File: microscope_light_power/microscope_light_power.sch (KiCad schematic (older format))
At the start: 36 parts, among them IC1 TPS61090, J1 MICROUSB, J2 5V175_out, J3 enable_switch, U1 MCP73871-2AA

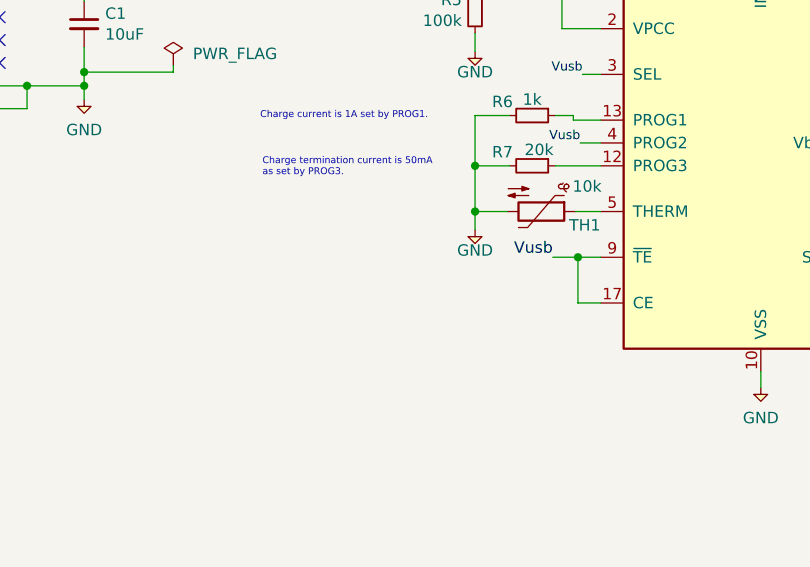
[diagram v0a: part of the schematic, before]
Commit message: Routed all of the direct connections from the MCP73871. I also added a note about the very bizarre routing for the thermistor. By the time I realized its trace would have to go on the bottom a good chunk of this board was routed. I routed it along the outside of the board to prevent breaking up the ground plane.
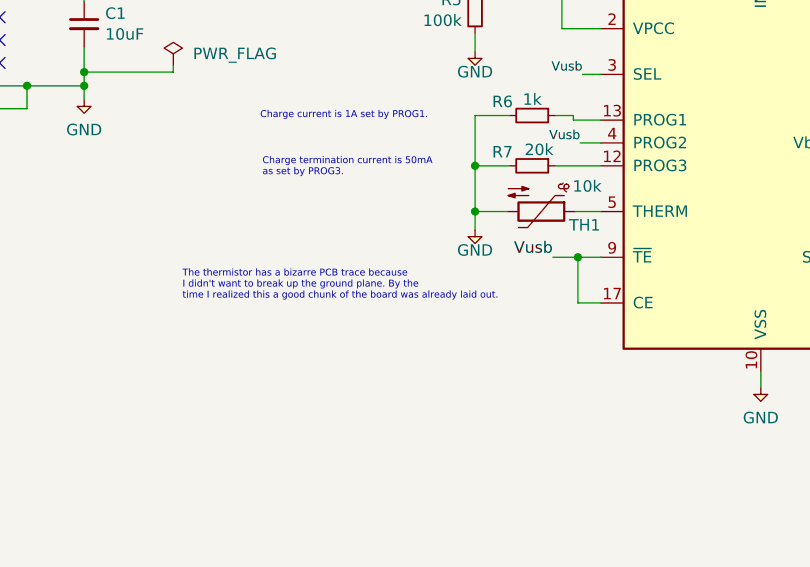
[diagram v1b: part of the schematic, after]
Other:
- note added: "The thermistor has a bizarre PCB trace because \nI didn't want to break up the ground plane. By the \ntime I realized this a good chunk of the board was already laid out."
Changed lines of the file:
@@
 Text Label 3250 4900 0    30   ~ 0
 SW
+Text Notes 2430 2750 0    30   ~ 0
+The thermistor has a bizarre PCB trace because \nI didn't want to break up the ground plane. By the \ntime I realized this a good chunk of the board was already laid out.
 $EndSCHEMATC

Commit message: Change the TPS61090 annotation from IC* to U* and move the reference designator on to the silkscreen layer.
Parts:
- renumbered IC1 to U2
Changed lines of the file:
@@
 $EndDescr
 $Comp
-L TPS61090 IC1
+L TPS61090 U2
 U 1 1 59D90497
 P 3700 5600
-F 0 "IC1" H 3700 6525 50  0000 C CNN
+F 0 "U2" H 3700 6525 50  0000 C CNN
 F 1 "TPS61090" H 3700 6434 50  0000 C CNN
 F 2 "agg:QFN-16-EP-TI" H 3400 4700 50  0001 L CNN

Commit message: Updated TPS61090 footprint to the correct footprint and modified the symbol to match KLC. sym-lib-table is due to a recent change in KiCad.
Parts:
- removed U2: TPS61090, agg:QFN-16-EP-TI, symbol TPS61090
- added U2: TPS61090, Housings_DFN_QFN:QFN-16-1EP_4x4mm_Pitch0.65mm, symbol dc-dc:TPS61090
- J1: symbol MICROUSB -> agg-kicad:MICROUSB
- J2, J3: symbol CONN_01x02 -> agg-kicad:CONN_01x02
- TP1, TP2, TP3, TP4: symbol TESTPAD -> agg-kicad:TESTPAD
- green1, yellow1: symbol LED -> agg-kicad:LED
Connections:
- wire segments 98 -> 99
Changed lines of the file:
@@
-EESchema Schematic File Version 3
-LIBS:agg-kicad
-LIBS:zetex
-LIBS:wiznet
-LIBS:triac_thyristor
-LIBS:nxp
-LIBS:modules
-LIBS:logic_programmable
-LIBS:intersil
-LIBS:infineon
-LIBS:driver_gate
-LIBS:bosch
-LIBS:bbd
-LIBS:Worldsemi
-LIBS:Valve
-LIBS:Transistor
-LIBS:Transformer
-LIBS:Switch
-LIBS:Sensor_Current
-LIBS:Relay
-LIBS:RFSolutions
-LIBS:Motor
-LIBS:Mechanical
-LIBS:MCU_Texas_MSP430
-LIBS:MCU_ST_STM8
-LIBS:MCU_ST_STM32
-LIBS:MCU_NXP_S08
-LIBS:MCU_NXP_LPC
-LIBS:MCU_NXP_Kinetis
-LIBS:MCU_Microchip_PIC32
-LIBS:MCU_Microchip_PIC24
-LIBS:MCU_Microchip_PIC18
-LIBS:MCU_Microchip_PIC16
-LIBS:MCU_Microchip_PIC12
-LIBS:MCU_Microchip_PIC10
-LIBS:Logic_TTL_IEEE
-LIBS:Logic_CMOS_IEEE
-LIBS:Logic_CMOS_4000
-LIBS:Logic_74xx
-LIBS:Logic_74xgxx
-LIBS:LEM
-LIBS:LED
-LIBS:Graphic
-LIBS:FPGA_Actel
-LIBS:Espressif
-LIBS:Display
-LIBS:Diode
-LIBS:DSP_Microchip_DSPIC33
-LIBS:Connector
-LIBS:Battery_Management
-LIBS:ftdi
-LIBS:intel
-LIBS:motor_drivers
-LIBS:references
-LIBS:maxim
-LIBS:opto
-LIBS:philips
-LIBS:pspice
-LIBS:xilinx
-LIBS:onsemi
-LIBS:digital-audio
-LIBS:interface
-LIBS:Oscillators
-LIBS:nordicsemi
-LIBS:sensors
-LIBS:contrib
-LIBS:video
-LIBS:ir
-LIBS:analog_switches
-LIBS:device
-LIBS:ESD_Protection
-LIBS:Altera
-LIBS:linear
-LIBS:atmel
-LIBS:supertex
-LIBS:siliconi
-LIBS:silabs
-LIBS:regul
-LIBS:memory
-LIBS:dsp
-LIBS:power
-LIBS:microchip
-LIBS:rfcom
-LIBS:ac-dc
-LIBS:Xicor
-LIBS:texas
-LIBS:Power_Management
-LIBS:hc11
-LIBS:analog_devices
-LIBS:dc-dc
-LIBS:powerint
-LIBS:elec-unifil
-LIBS:Zilog
-LIBS:adc-dac
-LIBS:motorola
-LIBS:Lattice
-LIBS:cypress
-LIBS:audio
-LIBS:microcontrollers
-LIBS:transistors
-LIBS:display
-LIBS:microchip_pic32mcu
-LIBS:microchip_dspic33dsc
-LIBS:conn
-LIBS:switches
-LIBS:graphic
-LIBS:nxp_armmcu
-LIBS:microchip_pic18mcu
-LIBS:74xgxx
-LIBS:cmos_ieee
-LIBS:diode
-LIBS:ttl_ieee
-LIBS:msp430
-LIBS:brooktre
-LIBS:microchip_pic10mcu
-LIBS:relays
-LIBS:stm8
-LIBS:valves
-LIBS:cmos4000
-LIBS:actel
-LIBS:stm32
-LIBS:logo
-LIBS:gennum
-LIBS:microchip_pic12mcu
-LIBS:74xx
-LIBS:transf
-LIBS:microchip_pic16mcu
+EESchema Schematic File Version 4
 LIBS:microscope_light_power-cache
 EELAYER 26 0
@@
 $EndDescr
 $Comp
-L TPS61090 U2
-U 1 1 59D90497
-P 3700 5600
-F 0 "U2" H 3700 6525 50  0000 C CNN
-F 1 "TPS61090" H 3700 6434 50  0000 C CNN
-F 2 "agg:QFN-16-EP-TI" H 3400 4700 50  0001 L CNN
-F 3 "http://www.ti.com/lit/ds/symlink/tps61090.pdf" H 3400 4600 50  0001 L CNN
-	1    3700 5600
-	1    0    0    -1
-$EndComp
-$Comp
 L MCP73871-2AA U1
 U 1 1 59D910F2
@@
 $EndComp
 $Comp
-L MICROUSB J1
+L agg-kicad:MICROUSB J1
 U 1 1 59D91D50
 P 1330 1610
@@
 $EndComp
 $Comp
-L GND #PWR01
+L agg-kicad:GND #PWR01
 U 1 1 59D99426
 P 2000 1870
@@
 Vusb
 $Comp
-L GND #PWR02
+L agg-kicad:GND #PWR02
 U 1 1 59D9AC2B
 P 3710 1660
@@
 $EndComp
 $Comp
-L GND #PWR03
+L agg-kicad:GND #PWR03
 U 1 1 59D9FB5D
 P 4960 3130
@@
 $EndComp
 $Comp
-L GND #PWR04
+L agg-kicad:GND #PWR04
 U 1 1 59DA04A7
 P 6480 2310
@@
 $EndComp
 $Comp
-L GND #PWR05
+L agg-kicad:GND #PWR05
 U 1 1 59DA245E
 P 3710 2440
@@
 Vusb
 $Comp
-L LED yellow1
+L agg-kicad:LED yellow1
 U 1 1 59DA5C71
 P 6050 2560
@@
 $EndComp
 $Comp
-L LED green1
+L agg-kicad:LED green1
 U 1 1 59DA7F2A
 P 6050 2660
@@
 $EndComp
 $Comp
-L GND #PWR06
+L agg-kicad:GND #PWR06
 U 1 1 59DCA58C
 P 6260 1750
@@
 enable
 $Comp
-L GND #PWR07
+L agg-kicad:GND #PWR07
 U 1 1 59EF0E02
 P 2330 5720
@@
 5V175
 $Comp
-L GND #PWR08
+L agg-kicad:GND #PWR08
 U 1 1 59F01C50
 P 4640 5610
@@
 $EndComp
 $Comp
-L GND #PWR09
+L agg-kicad:GND #PWR09
 U 1 1 59F0FE60
 P 2080 5260
@@
 $EndComp
 $Comp
-L GND #PWR010
+L agg-kicad:GND #PWR010
 U 1 1 59F358E1
 P 5200 5330
@@
 $EndComp
 $Comp
-L GND #PWR011
+L agg-kicad:GND #PWR011
 U 1 1 59F37EA3
-P 3130 6430
-F 0 "#PWR011" H 3000 6470 50  0001 L CNN
-F 1 "GND" H 3130 6297 50  0000 C CNN
-F 2 "" H 3130 6430 50  0001 C CNN
-F 3 "" H 3130 6430 50  0001 C CNN
-	1    3130 6430
+P 3750 6130
+F 0 "#PWR011" H 3620 6170 50  0001 L CNN
+F 1 "GND" H 3750 5997 50  0000 C CNN
+F 2 "" H 3750 6130 50  0001 C CNN
+F 3 "" H 3750 6130 50  0001 C CNN
+	1    3750 6130
 	1    0    0    -1
 $EndComp
@@
 	5200 5330 5200 5270
 Connection ~ 5200 5270
-Wire Wire Line
-	3300 5800 3130 5800
-Wire Wire Line
-	3130 5800 3130 6430
-Wire Wire Line
-	3300 5900 3130 5900
-Connection ~ 3130 5900
-Wire Wire Line
-	3300 6000 3130 6000
-Connection ~ 3130 6000
-Wire Wire Line
-	3300 6100 3130 6100
-Connection ~ 3130 6100
-Wire Wire Line
-	3300 6200 3130 6200
-Connection ~ 3130 6200
 $Comp
 L Mounting_Hole MK3
@@
 $EndComp
 $Comp
-L CONN_01x02 J3
+L agg-kicad:CONN_01x02 J3
 U 1 1 59FBD39A
 P 6370 5580
@@
 $EndComp
 $Comp
-L CONN_01x02 J2
+L agg-kicad:CONN_01x02 J2
 U 1 1 59FBD6E0
 P 6370 4900
@@
 $EndComp
 $Comp
-L GND #PWR012
+L agg-kicad:GND #PWR012
 U 1 1 59FC5FD9
 P 6200 5080
@@
 enable
 $Comp
-L GND #PWR013
+L agg-kicad:GND #PWR013
 U 1 1 59FCBF9F
 P 6190 5670
@@
 	6270 5480 6120 5480
 $Comp
-L TESTPAD TP2
+L agg-kicad:TESTPAD TP2
 U 1 1 59FD2D5E
 P 4400 5400
@@
 $EndComp
 $Comp
-L TESTPAD TP4
+L agg-kicad:TESTPAD TP4
 U 1 1 59FD7F8A
 P 6740 1410
@@
 $EndComp
 $Comp
-L TESTPAD TP1
+L agg-kicad:TESTPAD TP1
 U 1 1 59FD88E1
 P 2220 1410
@@
 Connection ~ 2000 1410
 $Comp
-L TESTPAD TP3
+L agg-kicad:TESTPAD TP3
 U 1 1 59FDA6BA
 P 6640 1860
@@
 Text Notes 2430 2750 0    30   ~ 0
 The thermistor has a bizarre PCB trace because \nI didn't want to break up the ground plane. By the \ntime I realized this a good chunk of the board was already laid out.
+Wire Wire Line
+	3500 6000 3500 6070
+Wire Wire Line
+	3500 6070 3900 6070
+Wire Wire Line
+	3900 6070 3900 6000
+Wire Wire Line
+	3600 6000 3600 6070
+Connection ~ 3600 6070
+Wire Wire Line
+	3700 6000 3700 6070
+Connection ~ 3700 6070
+Wire Wire Line
+	3800 6000 3800 6070
+Connection ~ 3800 6070
+Wire Wire Line
+	3750 6130 3750 6070
+Connection ~ 3750 6070
+$Comp
+L dc-dc:TPS61090 U2
+U 1 1 5A0D83DB
+P 3700 5400
+F 0 "U2" H 3700 6125 50  0000 C CNN
+F 1 "TPS61090" H 3700 6034 50  0000 C CNN
+F 2 "Housings_DFN_QFN:QFN-16-1EP_4x4mm_Pitch0.65mm" H 2750 4350 50  0001 L CNN
+F 3 "http://www.ti.com/lit/ds/symlink/tps61090.pdf" H 3850 4250 50  0001 L CNN
+	1    3700 5400
+	1    0    0    -1
+$EndComp
 $EndSCHEMATC

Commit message: The symbol library table update barfed and forgot which libraries all of my parts were in. I went through and manually added them back in.
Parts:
- BT1: symbol Battery_Cell -> device:Battery_Cell
- C1, C5, C6, C7: symbol C_Small -> device:C_Small
- C3: symbol CP1_Small -> device:CP1_Small
- L1: symbol L_Small -> device:L_Small
- MK1, MK2, MK3, MK4: symbol Mounting_Hole -> Mechanical:Mounting_Hole
- R10, R11, R4, R5, R6, R7: symbol R_Small -> device:R_Small
- TH1: symbol Thermistor_NTC -> device:Thermistor_NTC
- U1: symbol MCP73871-2AA -> Battery_Management:MCP73871-2AA
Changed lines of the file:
@@
 $EndDescr
 $Comp
-L MCP73871-2AA U1
+L Battery_Management:MCP73871-2AA U1
 U 1 1 59D910F2
 P 4960 2160
@@
 $EndComp
 $Comp
-L C_Small C1
+L device:C_Small C1
 U 1 1 59D98E5C
 P 2000 1540
@@
 Vusb
 $Comp
-L R_Small R4
+L device:R_Small R4
 U 1 1 59D9A07F
 P 3710 1120
@@
 $EndComp
 $Comp
-L R_Small R5
+L device:R_Small R5
 U 1 1 59D9A22F
 P 3710 1480
@@
 Vusb
 $Comp
-L Battery_Cell BT1
+L device:Battery_Cell BT1
 U 1 1 59D9D37D
 P 6480 2120
@@
 $EndComp
 $Comp
-L C_Small C6
+L device:C_Small C6
 U 1 1 59D9EDD9
 P 6160 2080
@@
 $EndComp
 $Comp
-L R_Small R6
+L device:R_Small R6
 U 1 1 59DA1BCD
 P 3960 1940
@@
 $EndComp
 $Comp
-L R_Small R10
+L device:R_Small R10
 U 1 1 59DA6091
 P 5860 2560
@@
 $EndComp
 $Comp
-L R_Small R11
+L device:R_Small R11
 U 1 1 59DA68A2
 P 5860 2660
@@
 Vusb
 $Comp
-L R_Small R7
+L device:R_Small R7
 U 1 1 59DADA49
 P 3960 2160
@@
 $EndComp
 $Comp
-L Thermistor_NTC TH1
+L device:Thermistor_NTC TH1
 U 1 1 59DBA795
 P 4000 2360
@@
 Vout
 $Comp
-L C_Small C5
+L device:C_Small C5
 U 1 1 59DC8009
 P 6150 1570
@@
 $EndComp
 $Comp
-L C_Small C7
+L device:C_Small C7
 U 1 1 59DC8053
 P 6390 1570
@@
 Charge termination current is 50mA \nas set by PROG3.
 $Comp
-L L_Small L1
+L device:L_Small L1
 U 1 1 59E33161
 P 3010 4900
@@
 $EndComp
 $Comp
-L CP1_Small C3
+L device:CP1_Small C3
 U 1 1 59F2FA52
 P 5020 5100
@@
 Connection ~ 5200 5270
 $Comp
-L Mounting_Hole MK3
+L Mechanical:Mounting_Hole MK3
 U 1 1 59FAECB9
 P 9290 1470
@@
 $EndComp
 $Comp
-L Mounting_Hole MK4
+L Mechanical:Mounting_Hole MK4
 U 1 1 59FAF2DD
 P 9290 1670
@@
 $EndComp
 $Comp
-L Mounting_Hole MK2
+L Mechanical:Mounting_Hole MK2
 U 1 1 59FAF43B
 P 9110 1670
@@
 $EndComp
 $Comp
-L Mounting_Hole MK1
+L Mechanical:Mounting_Hole MK1
 U 1 1 59FAF70C
 P 9110 1470
@@
 NoConn ~ 1630 1710
 $Comp
-L PWR_FLAG #FLG01
+L power:PWR_FLAG #FLG01
 U 1 1 59DCBD88
 P 2390 1720

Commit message: Continue unfucking library stuff after the symbol table update. Grumble grumble.
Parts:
- C2, C4: symbol C_Small -> device:C_Small
- R1, R2, R3, R8, R9: symbol R_Small -> device:R_Small
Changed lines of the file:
@@
 Vout
 $Comp
-L R_Small R2
+L device:R_Small R2
 U 1 1 59EDD7A4
 P 2330 5570
@@
 $EndComp
 $Comp
-L R_Small R1
+L device:R_Small R1
 U 1 1 59EDDA47
 P 2330 5270
@@
 Vout
 $Comp
-L R_Small R3
+L device:R_Small R3
 U 1 1 59EE2E52
 P 2840 5170
@@
 low_battery
 $Comp
-L R_Small R8
+L device:R_Small R8
 U 1 1 59EF7277
 P 4640 5120
@@
 $EndComp
 $Comp
-L R_Small R9
+L device:R_Small R9
 U 1 1 59EF7422
 P 4640 5450
@@
 $EndComp
 $Comp
-L C_Small C2
+L device:C_Small C2
 U 1 1 59F0D2BD
 P 2080 5100
@@
 $EndComp
 $Comp
-L C_Small C4
+L device:C_Small C4
 U 1 1 59F32F78
 P 5430 5100

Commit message: Remove rust firmware in favor of C/libopencm3 firmware for right now.
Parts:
- U2: symbol dc-dc:TPS61090 -> microscope_light_power-rescue:TPS61090-RESCUE-microscope_light_power
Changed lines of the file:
@@
 Connection ~ 3750 6070
 $Comp
-L dc-dc:TPS61090 U2
+L microscope_light_power-rescue:TPS61090-RESCUE-microscope_light_power U2
 U 1 1 5A0D83DB
 P 3700 5400
